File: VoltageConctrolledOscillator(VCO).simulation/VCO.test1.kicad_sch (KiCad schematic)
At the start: 28 parts, among them Q301 NMOS, U301 ${SIM.PARAMS}, U302 ${SIM.PARAMS}

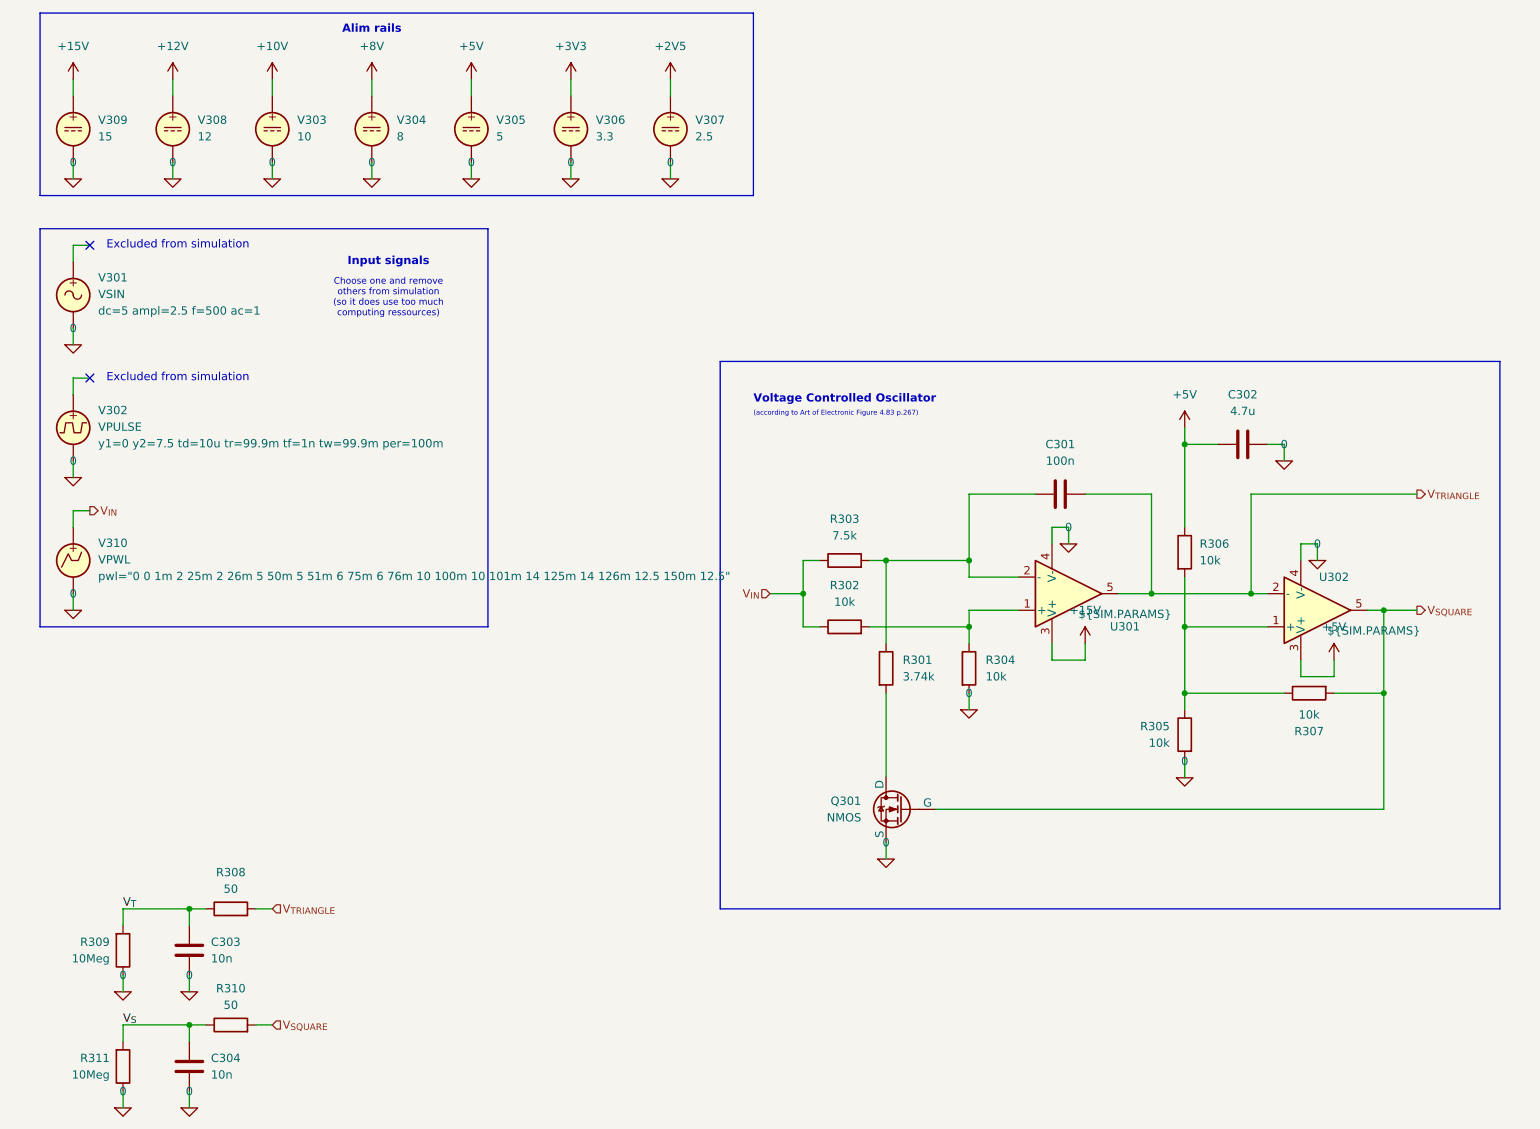
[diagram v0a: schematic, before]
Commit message: Rearrange sheets
Move stuff around sheets for future project evolution :
* Voltage sources are moved on top hierarchical page
* Hierarchical label is used to set input voltage to Test 1 sheet
* Add text on Test 0 sheet
* All subsheet page are A5 size for ease of read reason.
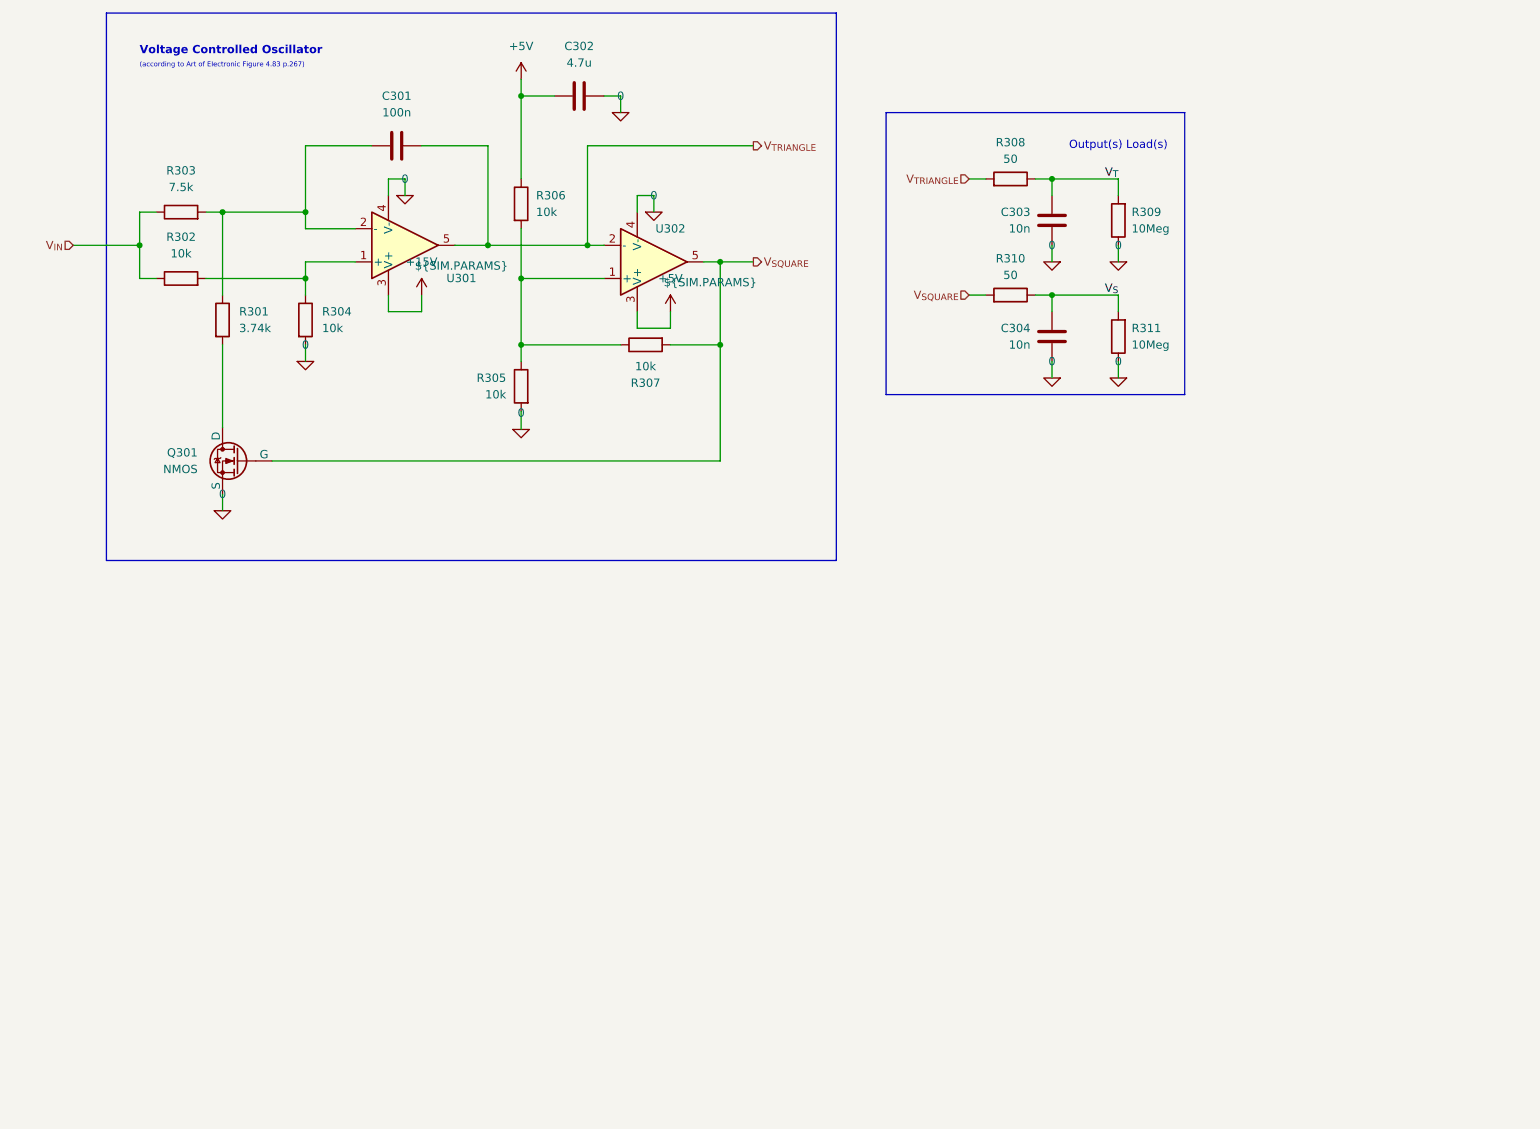
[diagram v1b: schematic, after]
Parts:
- removed V301: VSIN, symbol Simulation_SPICE:VSIN
- removed V302: VPULSE, symbol Simulation_SPICE:VPULSE
- removed V303: 10, symbol Simulation_SPICE:VDC
- removed V304: 8, symbol Simulation_SPICE:VDC
- removed V305: 5, symbol Simulation_SPICE:VDC
- removed V306: 3.3, symbol Simulation_SPICE:VDC
- removed V307: 2.5, symbol Simulation_SPICE:VDC
- removed V308: 12, symbol Simulation_SPICE:VDC
- removed V309: 15, symbol Simulation_SPICE:VDC
- removed V310: VPWL, symbol Simulation_SPICE:VPWL
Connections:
- no-connect marks 2 -> 0
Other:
- note added: "Output(s) Load(s)"
- note removed: "Alim rails"
- note removed: "Choose one and remove others from simulation (so it does use too much computing ressources)"
- note removed: "Excluded from simulation"
- note removed: "Input signals"
- moved on the sheet: C301, C302, C303, C304, Q301, R301, R302, R303, R304, R305, R306, R307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
